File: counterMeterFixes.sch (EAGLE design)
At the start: 128 parts, among them IC1 74AC14D, IC2 REG1117, IC3 74AC74D, IC4 74HC151D, IC5 74AC390D, IC6 74HC595D, IC7 74HC595D, J1 COMMON, J2 U/I/R, J3 10A, J4 U/I/R, K1 G6K-2P-Y, K2 G6K-2P-Y, K3 G6K-2P-Y, K4 G6K-2P-Y, K5 G6K-2P-Y, T1 BC847, T10 BC847, T2 BC847, T3 BC847, T4 BC847, T5 BC857, T6 BC857, T7 BC857, T8 BC857, T9 BC857, U1 MAX9201, U2 74XX161, U3 SN74LVC2G157DCTR, U4 MAX871, U5 AD8638, U6 AD8539

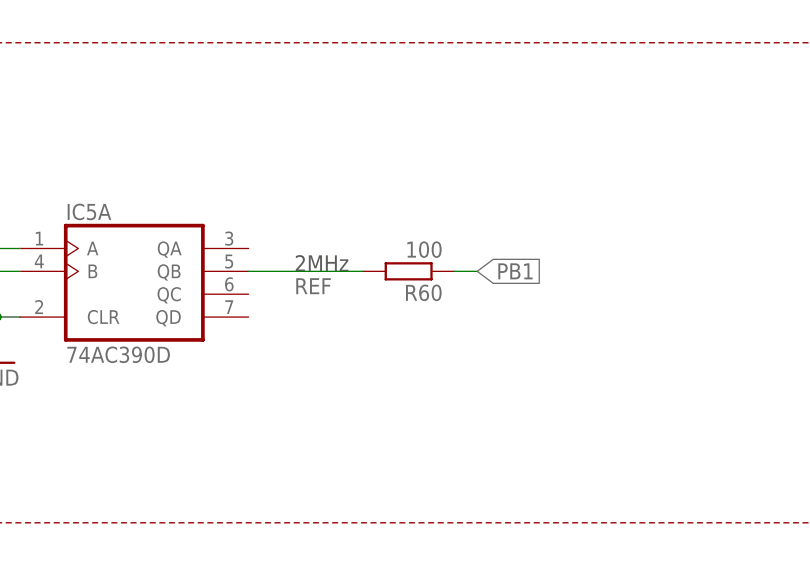
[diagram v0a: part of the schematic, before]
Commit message: corrected frequency division of reference signal IC5A Pin 6 instead of 5
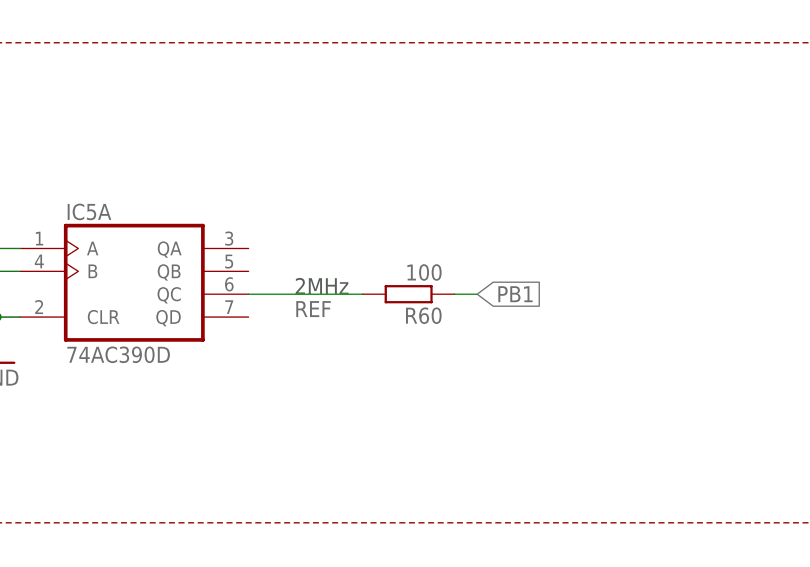
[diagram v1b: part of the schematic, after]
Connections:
- net REF: now also IC5A.QC; no longer IC5A.QB
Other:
- moved on the sheet: R60
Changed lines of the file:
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@@
 <text x="-38.1" y="-7.62" size="1.778" layer="94">100MHz (LF) input stage</text>
 <text x="-38.1" y="182.88" size="1.778" layer="94">LF/HF Multiplexer (optional)</text>
-<text x="88.9" y="27.94" size="1.778" layer="97">2MHz</text>
+<text x="88.9" y="25.4" size="1.778" layer="97">2MHz</text>
 <wire x1="317.5" y1="157.48" x2="317.5" y2="10.16" width="0.1524" layer="94" style="longdash"/>
 <wire x1="317.5" y1="10.16" x2="350.52" y2="10.16" width="0.1524" layer="94" style="longdash"/>
@@
 <instance part="R54" gate="G$1" x="284.48" y="53.34" rot="R180"/>
 <instance part="R56" gate="G$1" x="175.26" y="86.36" rot="R180"/>
-<instance part="R60" gate="G$1" x="101.6" y="27.94" rot="R180"/>
+<instance part="R60" gate="G$1" x="101.6" y="25.4" rot="R180"/>
 <instance part="IC6" gate="A" x="612.14" y="231.14"/>
 <instance part="IC7" gate="A" x="612.14" y="193.04"/>
@@
 <net name="REF" class="0">
 <segment>
-<pinref part="IC5" gate="A" pin="QB"/>
-<wire x1="83.82" y1="27.94" x2="96.52" y2="27.94" width="0.1524" layer="91"/>
-<label x="88.9" y="25.4" size="1.778" layer="95"/>
+<wire x1="83.82" y1="25.4" x2="96.52" y2="25.4" width="0.1524" layer="91"/>
+<label x="88.9" y="22.86" size="1.778" layer="95"/>
 <pinref part="R60" gate="G$1" pin="2"/>
+<pinref part="IC5" gate="A" pin="QC"/>
 </segment>
 </net>
@@
 <segment>
 <pinref part="R60" gate="G$1" pin="1"/>
-<wire x1="106.68" y1="27.94" x2="109.22" y2="27.94" width="0.1524" layer="91"/>
-<label x="109.22" y="27.94" size="1.778" layer="95" xref="yes"/>
-</segment>
-</net>
+<wire x1="106.68" y1="25.4" x2="109.22" y2="25.4" width="0.1524" layer="91"/>
+<label x="109.22" y="25.4" size="1.778" layer="95" xref="yes"/>
+</segment>
+</net>
